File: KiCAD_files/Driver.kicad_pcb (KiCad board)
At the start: 2 copper layers, 90 x 40 mm, 37 parts, among them J1 Driver_stage_outline_outputs, J2 Driver_stage_outline_inputs, U12 SFH617A-2X009T, U3 UCC21222DR, U4 UCC21222DR

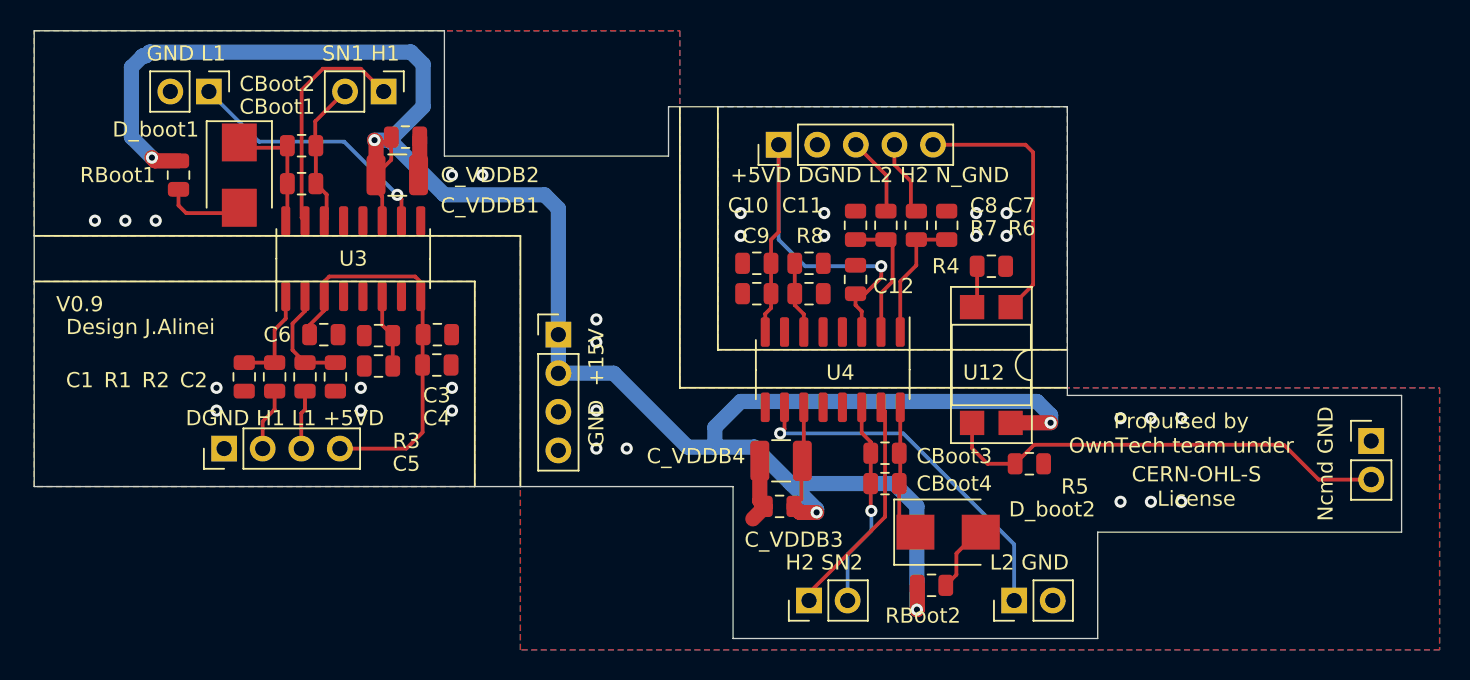
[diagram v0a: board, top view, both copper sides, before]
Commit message: Changed all the headers to improve mezzanine height
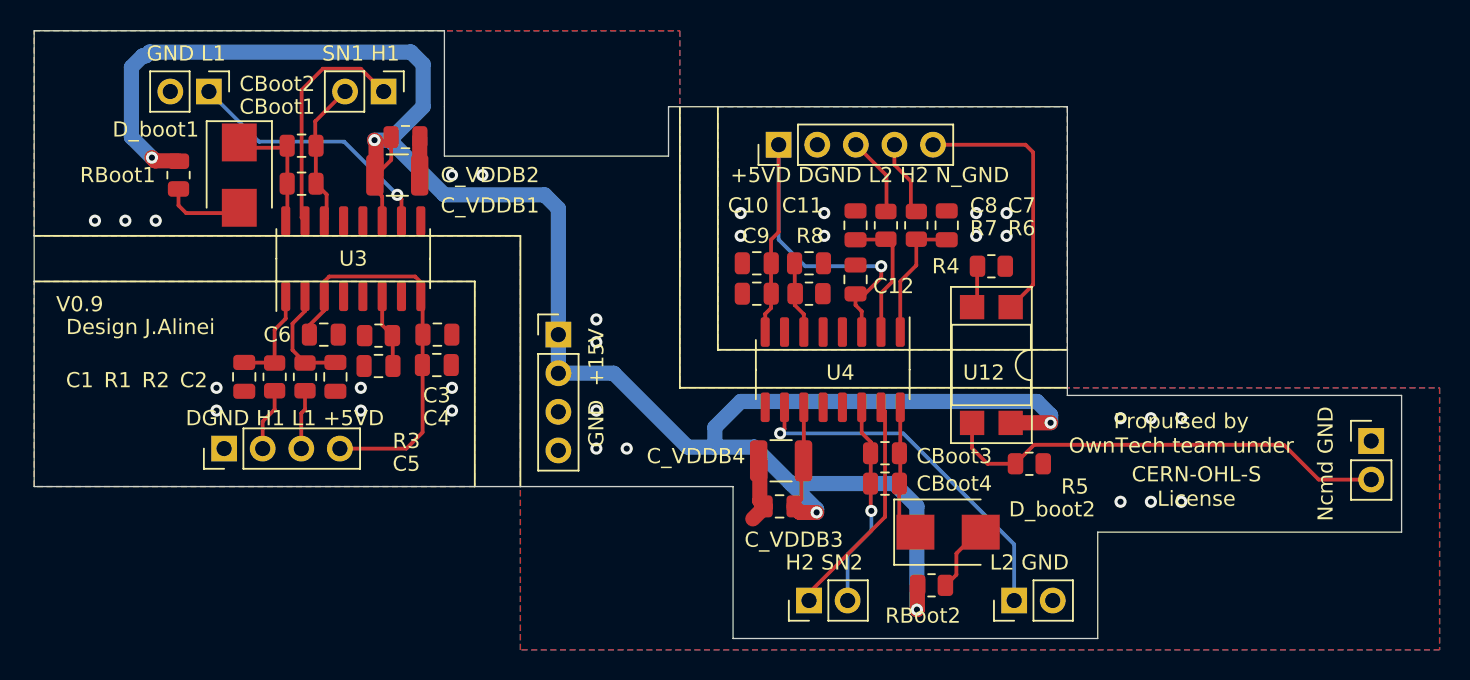
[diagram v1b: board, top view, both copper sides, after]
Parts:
- J1: value Driver_stage_outline_outputs -> Board outline
- J2: value Driver_stage_outline_inputs -> Driver_stage_outline
